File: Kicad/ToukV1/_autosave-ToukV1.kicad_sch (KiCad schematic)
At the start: 11 parts, among them J1 M1_T, J2 M2_T, SW10 SW_DPST_x2, SW11 SW_DPST_x2

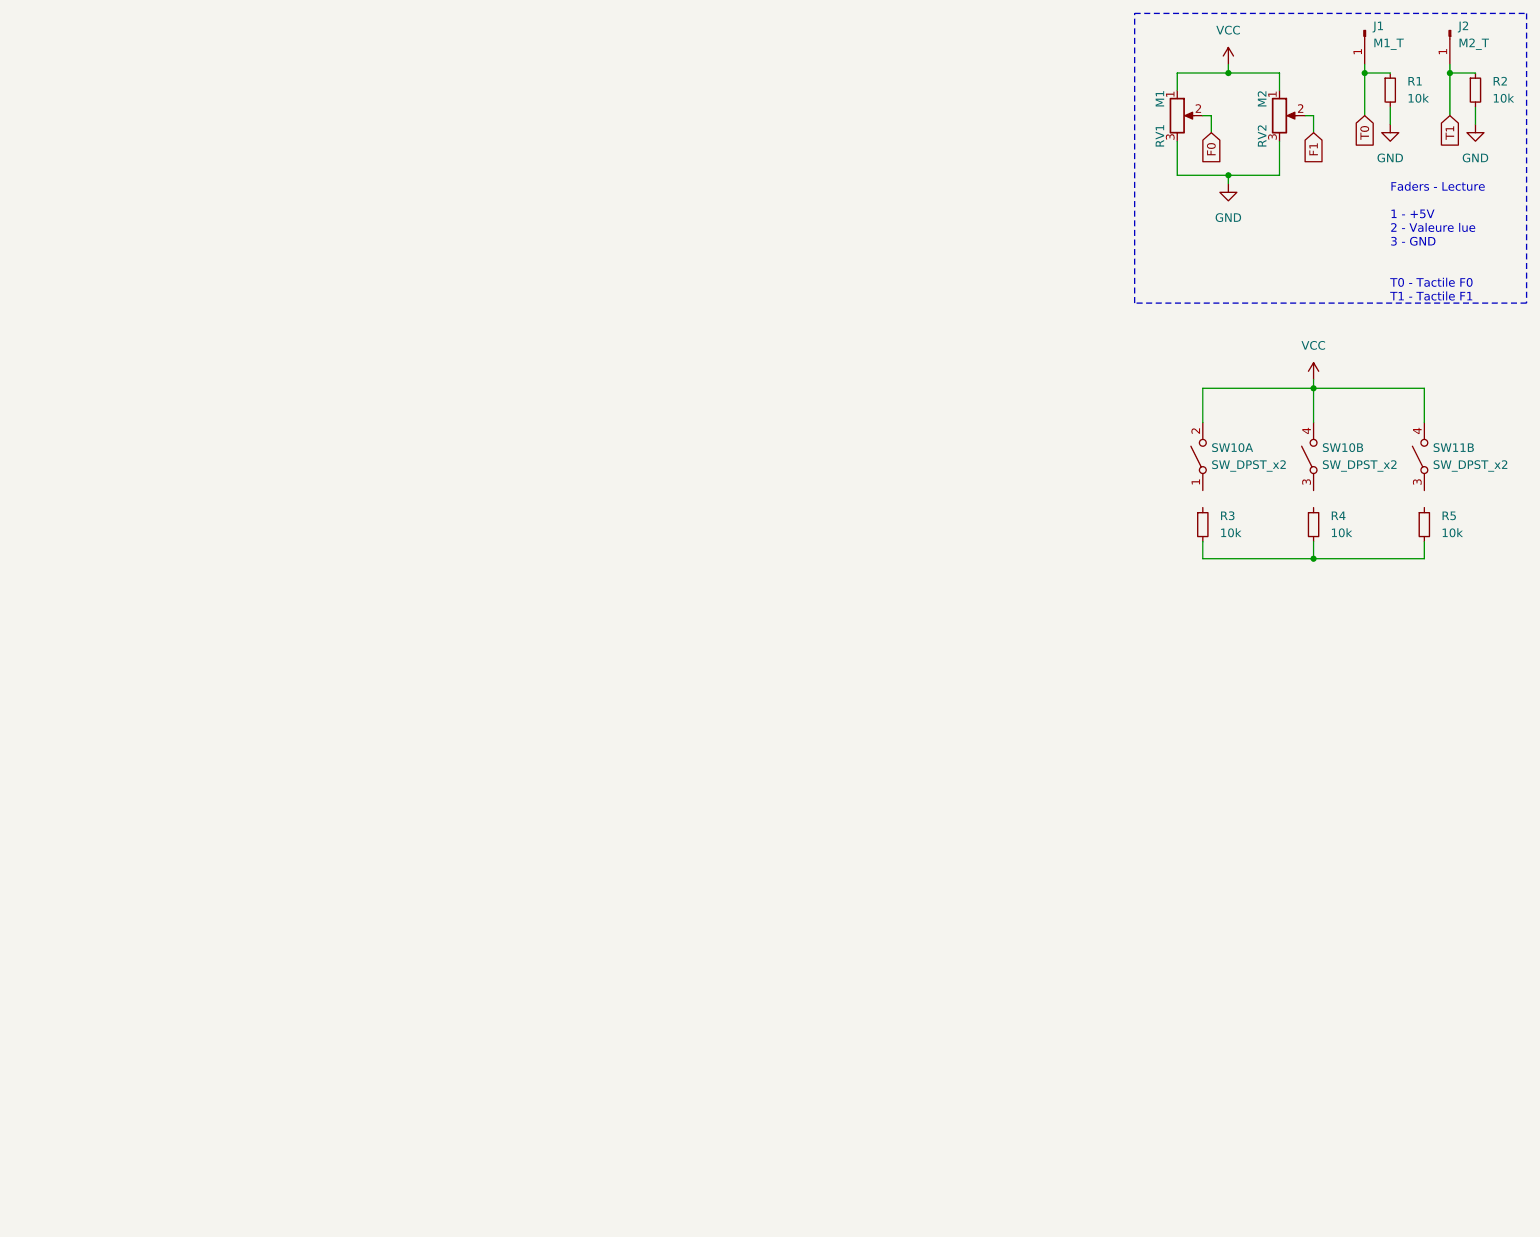
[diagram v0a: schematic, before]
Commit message: Ajout des Faders au Kicad
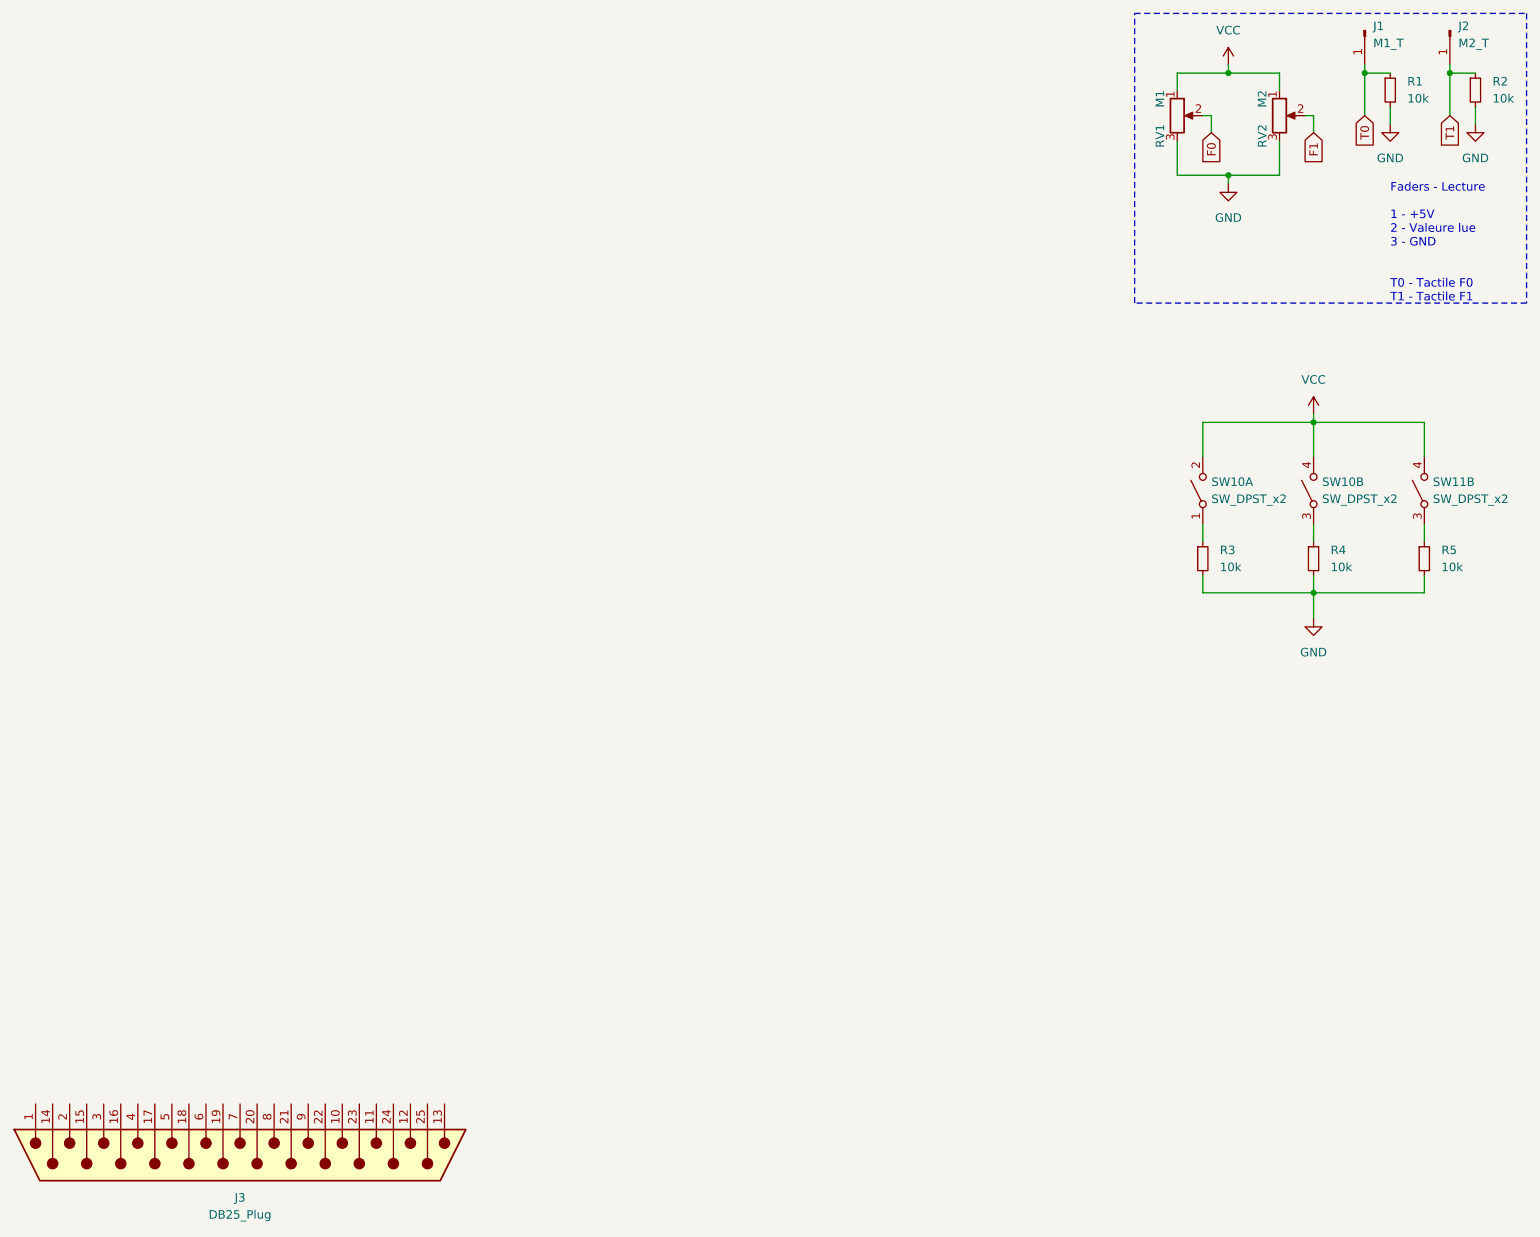
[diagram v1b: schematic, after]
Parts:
- added J3: DB25_Plug, symbol Connector:DB25_Plug
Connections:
- net GND: now also R3.2, R4.2, R5.2
- net at R4.1: now also SW10.3 (A)
- net at R3.1: now also SW10.1 (A)
- net at R5.1: now also SW11.3 (A)
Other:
- moved on the sheet: R3, R4, R5, SW10A, SW10B, SW11B
